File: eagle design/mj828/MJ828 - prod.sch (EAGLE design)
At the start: 28 parts, among them IC1 SFH 320 FA-Z, IC2 MAX6816EUS+T, IC3 ATTINY4313-MMH, IC4 AWSCR-8.00CELA-C10-T3, IC5 LDK320M50R, IC6 MCP2515, IC7 MCP2561-2

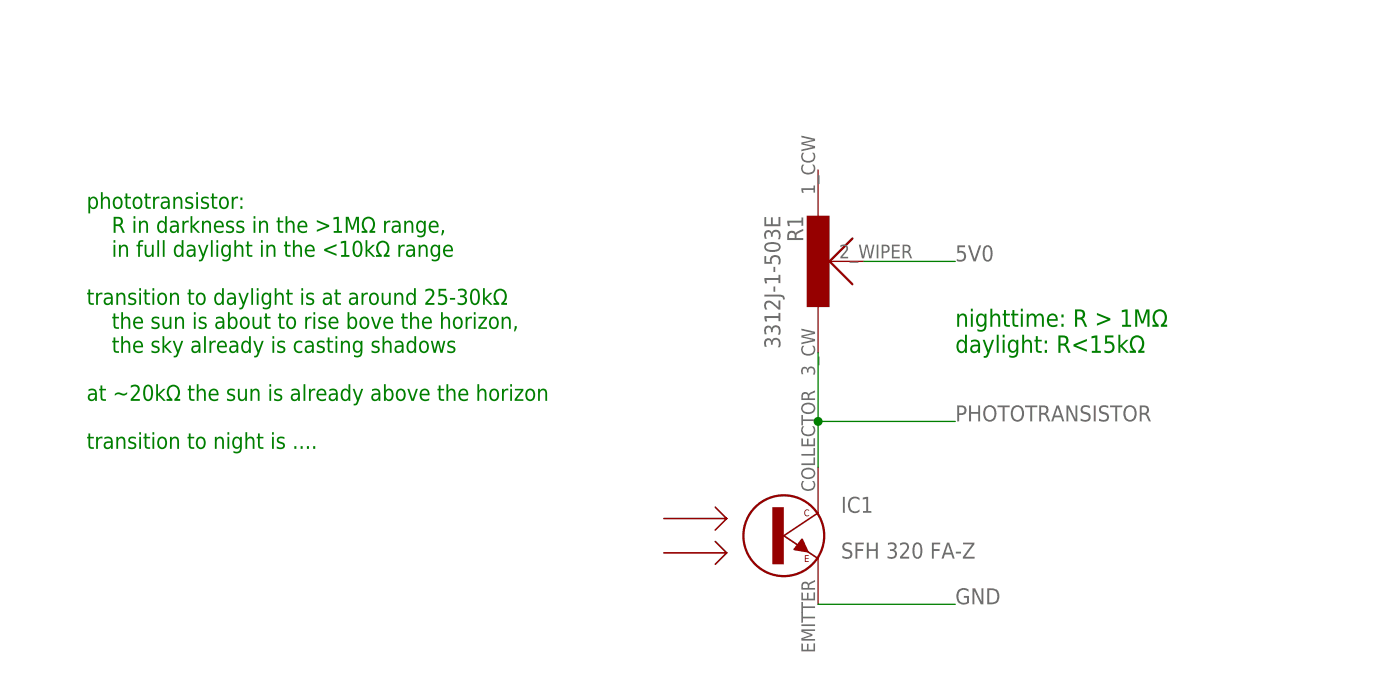
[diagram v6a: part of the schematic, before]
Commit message: - more observational data for the phototransistor
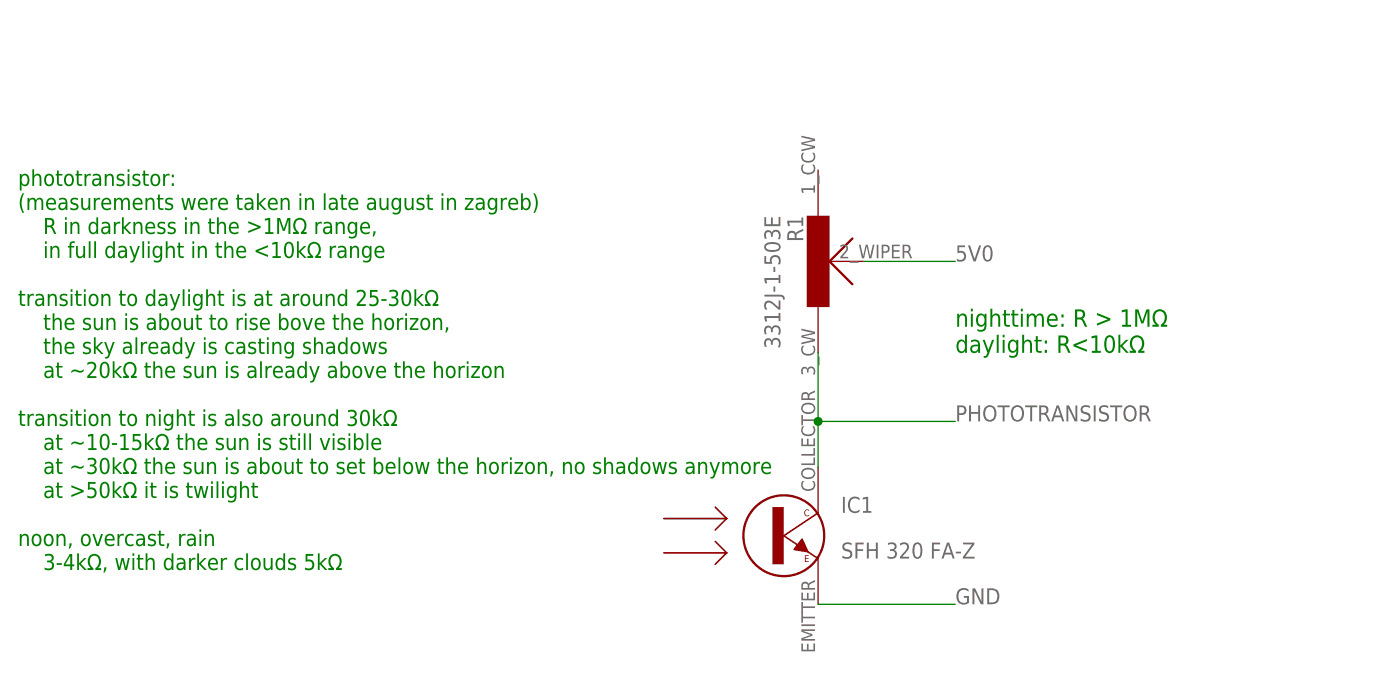
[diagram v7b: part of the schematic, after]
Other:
- note added: "nighttime: R > 1MΩ daylight: R<10kΩ"
- note added: "phototransistor: (measurements were taken in late august in zagreb) R in darkness in the >1MΩ range, in full daylight in the <10kΩ range transition to daylight is at around 25-30kΩ the sun is about to rise bove the horizon, the sky already is casting shadows at ~20kΩ the sun is already above the horizon transition to night is also around 30kΩ at ~10-15kΩ the sun is still visible at ~30kΩ the sun 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"
- note removed: "nighttime: R > 1MΩ daylight: R<15kΩ"
- note removed: "phototransistor: R in darkness in the >1MΩ range, in full daylight in the <10kΩ range transition to daylight is at around 25-30kΩ the sun is about to rise bove the horizon, the sky already is casting shadows at ~20kΩ the sun is already above the horizon transition to night is ...."
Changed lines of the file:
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@@
 <text x="231.14" y="195.58" size="1.778" layer="90">power supply for everything</text>
 <text x="261.62" y="78.74" size="1.778" layer="90">CAN infrastructure</text>
-<wire x1="2.54" y1="228.6" x2="81.28" y2="228.6" width="0.1524" layer="90"/>
+<wire x1="0" y1="228.6" x2="81.28" y2="228.6" width="0.1524" layer="90"/>
 <wire x1="81.28" y1="228.6" x2="307.34" y2="228.6" width="0.1524" layer="90"/>
 <wire x1="307.34" y1="228.6" x2="436.88" y2="228.6" width="0.1524" layer="90"/>
@@
 <wire x1="436.88" y1="101.6" x2="436.88" y2="0" width="0.1524" layer="90"/>
 <wire x1="436.88" y1="0" x2="81.28" y2="0" width="0.1524" layer="90"/>
-<wire x1="81.28" y1="0" x2="0" y2="0" width="0.1524" layer="90"/>
+<wire x1="81.28" y1="0" x2="-76.2" y2="0" width="0.1524" layer="90"/>
 <wire x1="81.28" y1="0" x2="81.28" y2="76.2" width="0.1524" layer="90"/>
 <wire x1="81.28" y1="76.2" x2="81.28" y2="101.6" width="0.1524" layer="90"/>
@@
 1.8V/0.02A=90Ω
 rounded to 100Ω</text>
-<text x="-53.34" y="58.42" size="1.778" layer="91" align="top-left">phototransistor:
+<text x="-60.96" y="60.96" size="1.778" layer="91" align="top-left">phototransistor:
+(measurements were taken in late august in zagreb)
     R in darkness in the &gt;1MΩ range,
     in full daylight in the &lt;10kΩ range
@@
     the sun is about to rise bove the horizon,
     the sky already is casting shadows
-at ~20kΩ the sun is already above the horizon
-transition to night is ....</text>
-<wire x1="0" y1="0" x2="-76.2" y2="0" width="0.1524" layer="90"/>
+    at ~20kΩ the sun is already above the horizon
+transition to night is also around 30kΩ
+    at ~10-15kΩ the sun is still visible
+    at ~30kΩ the sun is about to set below the horizon, no shadows anymore
+    at &gt;50kΩ it is twilight
+noon, overcast, rain
+    3-4kΩ, with darker clouds 5kΩ</text>
 <wire x1="-76.2" y1="0" x2="-76.2" y2="76.2" width="0.1524" layer="90"/>
 <wire x1="-76.2" y1="76.2" x2="0" y2="76.2" width="0.1524" layer="90"/>
 <wire x1="0" y1="76.2" x2="81.28" y2="76.2" width="0.1524" layer="90"/>
 <wire x1="0" y1="76.2" x2="0" y2="228.6" width="0.1524" layer="90"/>
-<wire x1="0" y1="228.6" x2="2.54" y2="228.6" width="0.1524" layer="90"/>
 <text x="170.18" y="180.34" size="5.08" layer="90">TODO: pulldown for brake/high beam signals</text>
 <text x="43.18" y="40.64" size="1.9304" layer="91">nighttime: R &gt; 1MΩ
-daylight: R&lt;15kΩ</text>
+daylight: R&lt;10kΩ</text>
 </plain>
 <instances>

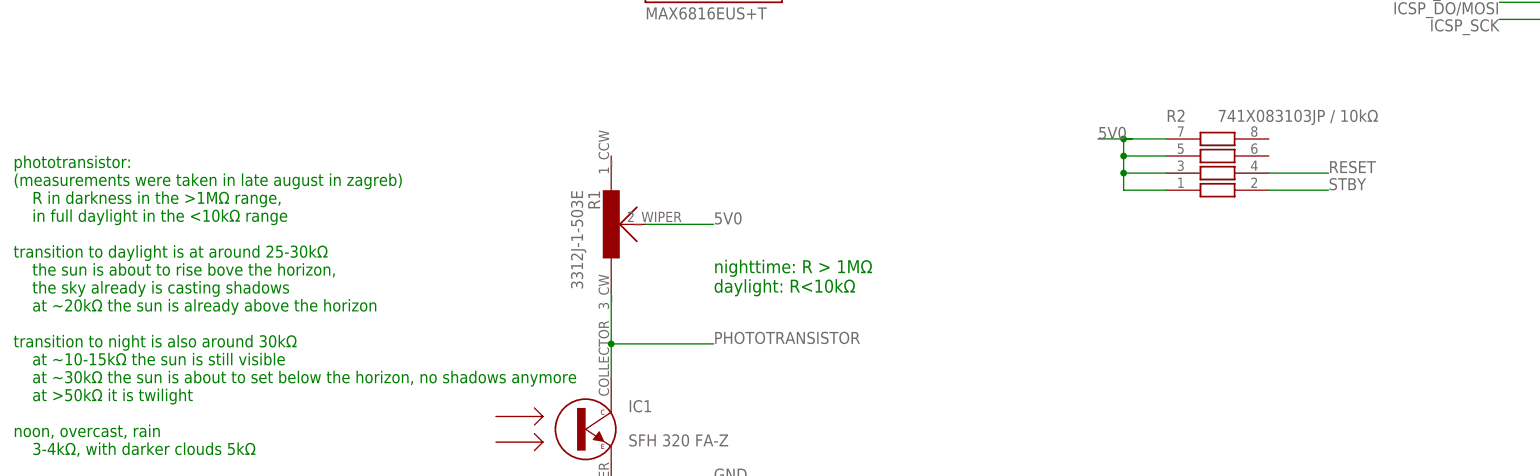
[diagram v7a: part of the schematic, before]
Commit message: - added pulldown to brake light and high beam pins
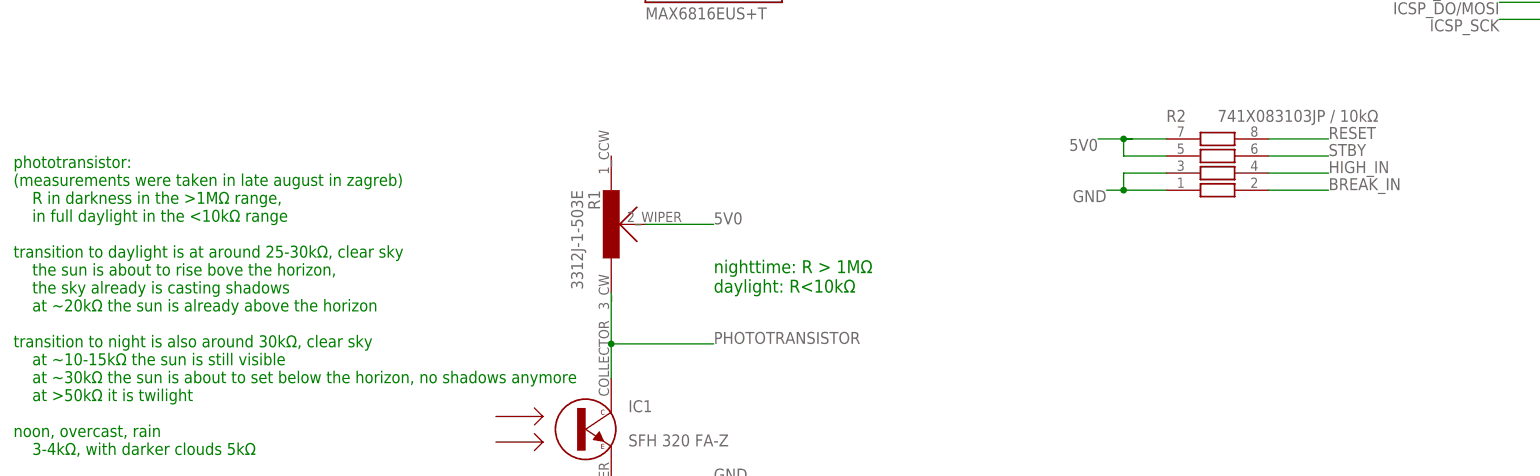
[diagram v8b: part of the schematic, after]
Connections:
- net 5V0: no longer R2.1, R2.3
- net BREAK_IN: now also R2.2
- net GND: now also R2.1, R2.3
- net HIGH_IN: now also R2.4
- net RESET: now also R2.8; no longer R2.4
- net STBY: now also R2.6; no longer R2.2
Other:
- note added: "phototransistor: (measurements were taken in late august in zagreb) R in darkness in the >1MΩ range, in full daylight in the <10kΩ range transition to daylight is at around 25-30kΩ, clear sky the sun is about to rise bove the horizon, the sky already is casting shadows at ~20kΩ the sun is already above the horizon transition to night is also around 30kΩ, clear sky at ~10-15kΩ the sun is still vis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"
- note removed: "phototransistor: (measurements were taken in late august in zagreb) R in darkness in the >1MΩ range, in full daylight in the <10kΩ range transition to daylight is at around 25-30kΩ the sun is about to rise bove the horizon, the sky already is casting shadows at ~20kΩ the sun is already above the horizon transition to night is also around 30kΩ at ~10-15kΩ the sun is still visible at ~30kΩ the sun 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"
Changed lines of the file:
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@@
     R in darkness in the &gt;1MΩ range,
     in full daylight in the &lt;10kΩ range
-transition to daylight is at around 25-30kΩ
+transition to daylight is at around 25-30kΩ, clear sky
     the sun is about to rise bove the horizon,
     the sky already is casting shadows
     at ~20kΩ the sun is already above the horizon
-transition to night is also around 30kΩ
+transition to night is also around 30kΩ, clear sky
     at ~10-15kΩ the sun is still visible
     at ~30kΩ the sun is about to set below the horizon, no shadows anymore
@@
 <label x="43.18" y="12.7" size="1.778" layer="95"/>
 </segment>
+<segment>
+<pinref part="R2" gate="G$1" pin="3"/>
+<wire x1="110.49" y1="58.42" x2="104.14" y2="58.42" width="0.1524" layer="91"/>
+<pinref part="R2" gate="G$1" pin="1"/>
+<wire x1="110.49" y1="55.88" x2="104.14" y2="55.88" width="0.1524" layer="91"/>
+<wire x1="104.14" y1="55.88" x2="104.14" y2="58.42" width="0.1524" layer="91"/>
+<wire x1="104.14" y1="55.88" x2="101.6" y2="55.88" width="0.1524" layer="91"/>
+<junction x="104.14" y="55.88"/>
+<label x="101.6" y="55.88" size="1.778" layer="95" rot="R180"/>
+</segment>
 </net>
 <net name="ICSP_DO/MOSI" class="3">
@@
 </segment>
 <segment>
-<pinref part="R2" gate="G$1" pin="2"/>
-<wire x1="125.73" y1="55.88" x2="134.62" y2="55.88" width="0.1524" layer="91"/>
-<label x="134.62" y="55.88" size="1.778" layer="95"/>
-</segment>
-<segment>
 <pinref part="IC3" gate="G$1" pin="PCINT17/ICPI-PD6"/>
 <wire x1="157.48" y1="185.42" x2="162.56" y2="185.42" width="0.1524" layer="91"/>
 <label x="162.56" y="185.42" size="1.778" layer="95"/>
+</segment>
+<segment>
+<pinref part="R2" gate="G$1" pin="6"/>
+<wire x1="125.73" y1="60.96" x2="134.62" y2="60.96" width="0.1524" layer="91"/>
+<label x="134.62" y="60.96" size="1.778" layer="95"/>
 </segment>
 </net>
@@
 </segment>
 <segment>
-<label x="100.33" y="63.5" size="1.778" layer="95"/>
+<label x="100.33" y="63.5" size="1.778" layer="95" rot="R180"/>
 <wire x1="105.41" y1="63.5" x2="104.14" y2="63.5" width="0.1524" layer="91"/>
 <wire x1="104.14" y1="63.5" x2="100.33" y2="63.5" width="0.1524" layer="91"/>
@@
 <pinref part="R2" gate="G$1" pin="7"/>
 <wire x1="110.49" y1="63.5" x2="104.14" y2="63.5" width="0.1524" layer="91"/>
-<pinref part="R2" gate="G$1" pin="3"/>
-<wire x1="110.49" y1="58.42" x2="104.14" y2="58.42" width="0.1524" layer="91"/>
-<wire x1="104.14" y1="58.42" x2="104.14" y2="60.96" width="0.1524" layer="91"/>
-<junction x="104.14" y="60.96"/>
-<pinref part="R2" gate="G$1" pin="1"/>
-<wire x1="110.49" y1="55.88" x2="104.14" y2="55.88" width="0.1524" layer="91"/>
-<wire x1="104.14" y1="55.88" x2="104.14" y2="58.42" width="0.1524" layer="91"/>
-<junction x="104.14" y="58.42"/>
 </segment>
 <segment>
@@
 </segment>
 <segment>
-<pinref part="R2" gate="G$1" pin="4"/>
-<wire x1="125.73" y1="58.42" x2="134.62" y2="58.42" width="0.1524" layer="91"/>
-<label x="134.62" y="58.42" size="1.778" layer="95"/>
+<pinref part="R2" gate="G$1" pin="8"/>
+<wire x1="125.73" y1="63.5" x2="134.62" y2="63.5" width="0.1524" layer="91"/>
+<label x="134.62" y="63.5" size="1.778" layer="95"/>
 </segment>
 </net>
@@
 <label x="45.72" y="157.48" size="1.778" layer="95"/>
 </segment>
+<segment>
+<pinref part="R2" gate="G$1" pin="2"/>
+<wire x1="125.73" y1="55.88" x2="134.62" y2="55.88" width="0.1524" layer="91"/>
+<label x="134.62" y="55.88" size="1.778" layer="95"/>
+</segment>
 </net>
 <net name="HIGH_IN" class="3">
@@
 <label x="45.72" y="154.94" size="1.778" layer="95"/>
 </segment>
-</net>
+<segment>
+<pinref part="R2" gate="G$1" pin="4"/>
+<wire x1="125.73" y1="58.42" x2="134.62" y2="58.42" width="0.1524" layer="91"/>
+<label x="134.62" y="58.42" size="1.778" layer="95"/>
+</segment>
+</net>
